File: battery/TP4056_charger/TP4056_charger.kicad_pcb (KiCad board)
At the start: 2 copper layers, 19 parts

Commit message: separate charger and battery
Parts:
- removed BAT_J1: BATT, ErgoCai.pretty:JST_PH_S2B-PH-K_1x02_P2.00mm_Horizontal

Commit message: update e-papert
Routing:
- net VBAT: track 17.6 -> 7.25 mm
- net GND: track 43.5 -> 40.9 mm, vias 1 -> 2
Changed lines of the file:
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@@
 	)
 	(segment
-		(start -1.02 16.99)
-		(end -1.02 4.82)
+		(start 2.35 1.45)
+		(end -0.18 3.98)
 		(width 0.2)
 		(layer "F.Cu")
@@
 	)
 	(segment
-		(start -1.02 4.82)
-		(end 2.35 1.45)
+		(start -0.18 3.98)
+		(end -0.18 15.83)
 		(width 0.2)
 		(layer "F.Cu")
+		(net 1)
+	)
+	(via
+		(at -0.18 15.83)
+		(size 0.6)
+		(drill 0.3)
+		(layers "F.Cu" "B.Cu")
 		(net 1)
 	)
@@
 	)
 	(segment
-		(start -1.15 16.86)
-		(end -1.02 16.99)
-		(width 0.2)
-		(layer "B.Cu")
-		(net 1)
-	)
-	(segment
 		(start -4.452 9.895)
 		(end -3.95 9.895)
@@
 	)
 	(segment
+		(start -1.15 14.86)
+		(end -0.18 15.83)
+		(width 0.2)
+		(layer "B.Cu")
+		(net 1)
+	)
+	(segment
 		(start -2.65 6.67)
 		(end -2.65 9.445)
@@
 	)
 	(segment
-		(start -1.15 16.425)
-		(end -0.96 16.615)
-		(width 0.2)
-		(layer "B.Cu")
-		(net 1)
-	)
-	(segment
 		(start 2.35 2.7325)
 		(end 0.85 4.2325)
@@
 	)
 	(segment
+		(start -1.15 14.72)
+		(end -1.15 14.86)
+		(width 0.2)
+		(layer "B.Cu")
+		(net 1)
+	)
+	(segment
 		(start 0.85 4.2375)
 		(end 0.85 5.8375)
@@
 	)
 	(segment
-		(start -1.15 14.72)
-		(end -1.15 16.86)
-		(width 0.2)
-		(layer "B.Cu")
-		(net 1)
-	)
-	(segment
 		(start -4.926 10.369)
 		(end -4.452 9.895)
@@
 	)
 	(segment
-		(start 6.126 15.1351)
-		(end 6.126 12.2535)
-		(width 0.2)
-		(layer "B.Cu")
-		(net 13)
-	)
-	(segment
 		(start 5.35 4.2325)
 		(end 5.606 4.4885)
@@
 		(width 0.2)
 		(layer "B.Cu")
-		(net 13)
-	)
-	(segment
-		(start 6.126 12.2535)
-		(end 5.005 11.1325)
-		(width 0.2)
-		(layer "B.Cu")
-		(net 13)
-	)
-	(segment
-		(start 4.2711 16.99)
-		(end 6.126 15.1351)
-		(width 0.2)
-		(layer "B.Cu")
-		(net 13)
-	)
-	(segment
-		(start 0.98 16.99)
-		(end 4.2711 16.99)
-		(width 0.2)
-		(layer "B.Cu")

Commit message: remove vin in charger
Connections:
- net VIN renamed Net-(BAT_D1-K)
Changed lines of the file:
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@@
 	(net 8 "Net-(BAT_TP1-~{CHRG})")
 	(net 9 "Net-(BAT_TP1-PROG)")
-	(net 10 "VIN")
+	(net 10 "Net-(BAT_D1-K)")
 	(net 11 "Net-(BAT_U1-FB)")
 	(net 12 "Net-(BAT_U1-LX)")
@@
 			(layers "B.Cu" "B.Mask" "B.Paste")
 			(roundrect_rratio 0.25)
-			(net 10 "VIN")
+			(net 10 "Net-(BAT_D1-K)")
 			(pinfunction "S")
 			(pintype "passive")
@@
 			(layers "B.Cu" "B.Mask" "B.Paste")
 			(roundrect_rratio 0.25)
-			(net 10 "VIN")
+			(net 10 "Net-(BAT_D1-K)")
 			(pintype "passive")
 		)
@@
 			(layers "B.Cu" "B.Mask" "B.Paste")
 			(roundrect_rratio 0.25)
-			(net 10 "VIN")
+			(net 10 "Net-(BAT_D1-K)")
 			(pinfunction "K")
 			(pintype "passive")
@@
 			(size 1.1 0.6)
 			(layers "B.Cu" "B.Mask" "B.Paste")
-			(net 10 "VIN")
+			(net 10 "Net-(BAT_D1-K)")
 			(pinfunction "EN")
 			(pintype "unspecified")
@@
 			(size 1.1 0.6)
 			(layers "B.Cu" "B.Mask" "B.Paste")
-			(net 10 "VIN")
+			(net 10 "Net-(BAT_D1-K)")
 			(pinfunction "IN")
 			(pintype "unspecified")

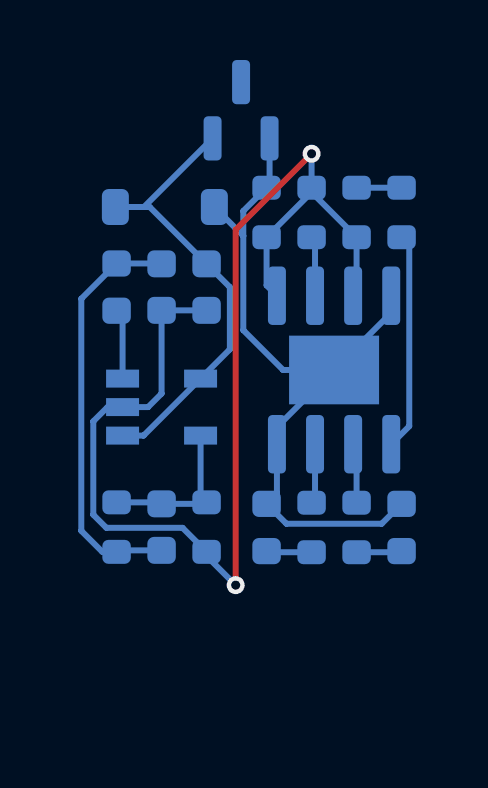
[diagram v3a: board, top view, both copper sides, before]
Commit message: update TP4056 charger
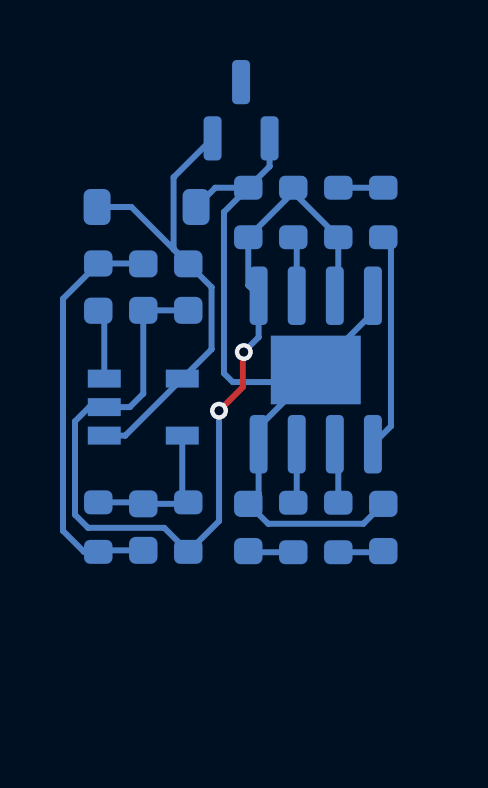
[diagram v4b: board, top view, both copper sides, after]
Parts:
- moved BAT_C1 0.61 mm to (-1.76, 5.89)
- moved BAT_R2 0.61 mm to (-1.76, 13.9)
- moved BAT_R_LEDR1 0.61 mm to (1.74, 13.9)
- moved BAT_R_P1 0.61 mm to (1.74, 3.41)
- moved BAT_LEDR1 0.61 mm to (0.24, 13.9)
- moved BAT_R_G1 0.61 mm to (0.24, 3.41)
- moved BAT_C2 0.61 mm to (-3.26, 13.9)
- moved BAT_C3 0.61 mm to (-3.26, 5.89)
- moved BAT_D1 0.61 mm to (-3.15, 3.23)
- moved BAT_RB1 0.61 mm to (3.24, 3.41)
- moved BAT_R_LEDB1 0.61 mm to (3.24, 13.9)
- moved BAT_TP1 0.61 mm to (2.49, 8.66)
- moved BAT_U1 0.61 mm to (-3.26, 9.89)
- moved BAT_L1 0.61 mm to (-4.76, 5.89)
- moved BAT_LEDB1 0.61 mm to (4.74, 13.9)
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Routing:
- net GND: track 40.9 -> 32.5 mm
- net VBUS: track 25.4 -> 27.5 mm
- net Net-(BAT_D1-K): track 16.0 -> 17.6 mm
